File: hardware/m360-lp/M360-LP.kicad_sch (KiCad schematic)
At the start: 53 parts, among them J1 RJ45 SOLO, J2 RJ45 CLIMA/AUX, J3 J_VIN 3,0-6V, J4 M360-RF, Q1 AO3401A, Q2 AO3401A, SW1 Reed, U1 MCP1700T-3302E/TT, U2 74HC4051, U3 SRV05-4, U4 SRV05-4, U5 SRV05-4

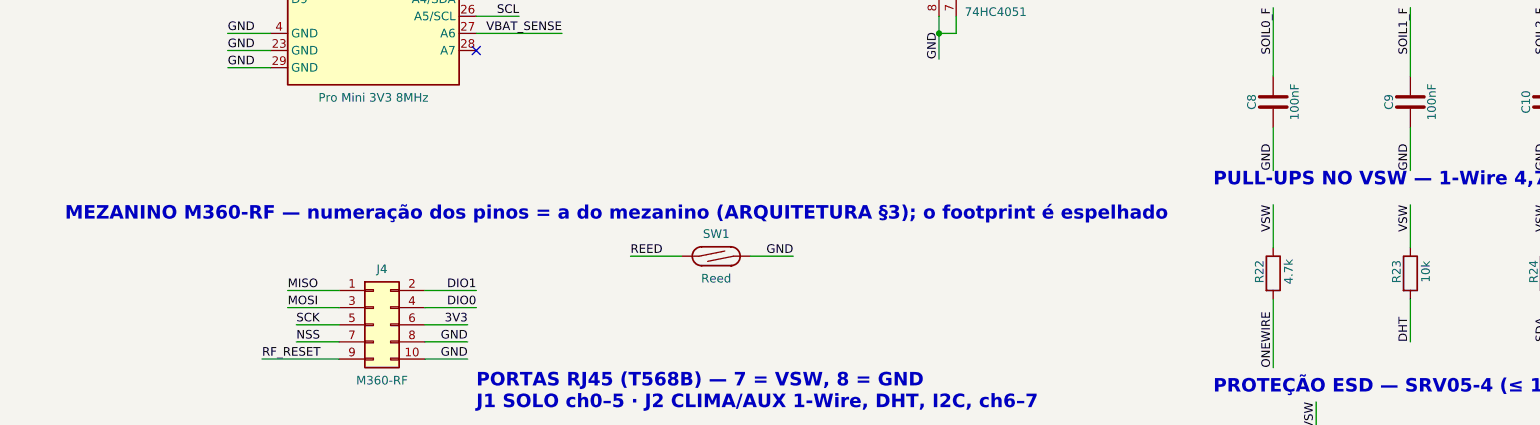
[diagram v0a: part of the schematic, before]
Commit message: feat(hardware): footprints da família e posicionamento da M360-LP na caixa
Biblioteca hardware/lib/M360.pretty com os quatro footprints que faltavam: Pro Mini,
soquete do mezanino, RJ45 (C385834) e reed (C315909). Os dois últimos vieram do LCSC pelo
easyeda2kicad, com os pinos-guia do RJ45 corrigidos para furo não metalizado e o modelo 3D
subido 6,3 mm — vinha atravessando a placa. O datasheet confirma conector comum: corpo de
12,6 mm apoiado na face e pinos de 3,0 mm.

O soquete do mezanino não precisa ser espelhado: o PinSocket stock já tem a coluna par em x
negativo, o mesmo lado em que ela fica no J1 do mezanino, que é montado na face de baixo.
Esquemático e documento corrigidos.

Furos livres do Pro Mini medidos por foto (docs/prominiFront.jpg), por homografia a partir
de quatro pinos de canto de posição conhecida (passo 2,54 mm, fileiras a 15,24 mm; escala
consistente em 2% nas quatro bordas): A5 em (12,70; 8,89), A4 em (12,70; 11,43) e GND/A6/A7
em x = 7,62/10,16/12,70 com y = 28,3 ± 0,3. Os espaçamentos medidos (2,57 e 2,59 mm)
confirmam a grade de 2,54. Esses cinco furos levam 1,2 mm — e não 1,0 — para absorver a
incerteza da medição; confirmar com paquímetro antes de fabricar.

Posicionamento em 86 × 62 mm, formato imposto pela caixa de 100 × 100 × 50 mm: o plugue
RJ45 é crimpado dentro da caixa e pede ~25-30 mm livres à frente dos conectores, com os
prensa-cabos na parede em frente. RJ45 e reed na borda de baixo, TVS logo atrás deles,
matriz RC dos 8 canais no meio, Pro Mini deitado com o header FTDI para fora da borda
esquerda, mezanino no alto à direita com o SMA pela borda e a alimentação embaixo dele
(~11 mm livres, só SMD baixo). DRC sem sobreposição de courtyard nem erro de isolamento;
faltam o roteamento e o acerto de serigrafia dos textos de U2, U4 e U5.

Co-Authored-By: Claude Opus 5 (1M context) <noreply@anthropic.com>
Claude-Session: https://claude.ai/code/session_01G3CpSsqAsoKgMUYE5MhRV7
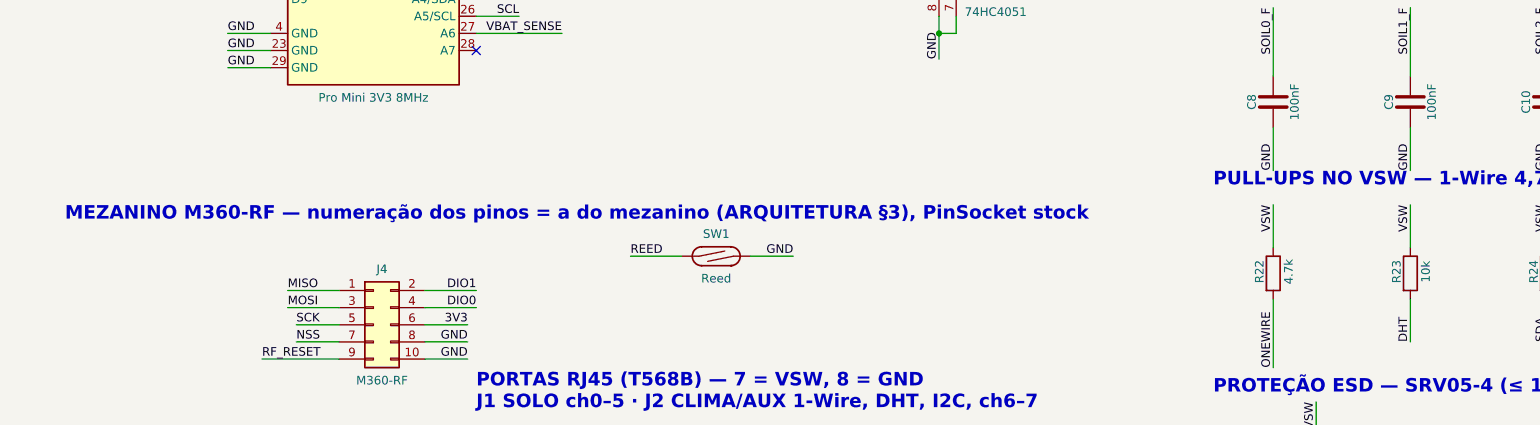
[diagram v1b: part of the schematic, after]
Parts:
- A1: footprint (none) -> M360:Arduino_ProMini_DeeKRobot
- J1, J2: footprint (none) -> M360:RJ45_R-RJ45R08P-A004
- J4: footprint (none) -> M360:M360-RF_Soquete_2x05
- SW1: footprint (none) -> M360:Reed_Littelfuse_59170
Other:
- note added: "MEZANINO M360-RF — numeração dos pinos = a do mezanino (ARQUITETURA §3), PinSocket stock"
- note removed: "MEZANINO M360-RF — numeração dos pinos = a do mezanino (ARQUITETURA §3); o footprint é espelhado"
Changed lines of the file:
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@@
 		(company "M360 Horta")
 		(comment 1 "Arquitetura: hardware/ARQUITETURA_FAMILIA.md §4 e §7")
-		(comment 2 "Footprints pendentes: A1 Pro Mini, J1/J2 RJ45, J4 soquete espelhado, SW1 reed")
+		(comment 2 "Footprints em hardware/lib/M360.pretty; furos A4–A7 do Pro Mini a medir")
 	)
-	(text "MEZANINO M360-RF — numeração dos pinos = a do mezanino (ARQUITETURA §3); o footprint é espelhado"
+	(text "MEZANINO M360-RF — numeração dos pinos = a do mezanino (ARQUITETURA §3), PinSocket stock"
 		(exclude_from_sim no)
 		(at 30.48 185.42 0)
@@
 			)
 		)
-		(property "Footprint" ""
+		(property "Footprint" "M360:M360-RF_Soquete_2x05"
 			(at 76.2 200.66 0)
 			(hide yes)
@@
 			)
 		)
-		(property "Footprint" ""
+		(property "Footprint" "M360:RJ45_R-RJ45R08P-A004"
 			(at 111.76 239.395 90)
 			(hide yes)
@@
 			)
 		)
-		(property "Footprint" ""
+		(property "Footprint" "M360:RJ45_R-RJ45R08P-A004"
 			(at 157.48 239.395 90)
 			(hide yes)
@@
 			)
 		)
-		(property "Footprint" ""
+		(property "Footprint" "M360:Arduino_ProMini_DeeKRobot"
 			(at 76.2 134.62 0)
 			(hide yes)
@@
 			)
 		)
-		(property "Footprint" ""
+		(property "Footprint" "M360:Reed_Littelfuse_59170"
 			(at 127 190.5 0)
 			(hide yes)

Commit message: feat(hardware): reed vira botão na LP e na ACT — esquemático apenas
⚠️ **ENTREGA PARCIAL: as placas NÃO acompanham.** Os dois `.kicad_pcb` continuam com o reed
`M360:Reed_Littelfuse_59170`. Sincronizar esquemático → placa vai trocar o footprint e
**invalidar o roteamento das duas** (§11.5). Não faça isso sem estar pronto para rerrotear.

O que entra aqui:

- SW1 passa de `Switch:SW_Reed` para `Switch:SW_Push`, footprint
  `Button_Switch_THT:SW_PUSH_6mm`, valor "Repareamento". Os dois símbolos têm pinagem e
  geometria idênticas (pinos 1 e 2 em ±5,08), então a troca não pode alterar a fiação — e o
  `netdiff.py` confirmou: LP 47 redes/182 nós e ACT 63/166, idênticas à base nas duas;
- `place_lp.py`: SW1 de (160, 158) para (160, 153) — o botão ocupa 9,6 × 7,6 mm contra
  11,5 × 2,4 do reed e, em 158, avançaria até y ≈ 164, além da borda em 162;
- `place_act.py`: SW1 sem rotação, e **J1 de rot 90 para rot 0**. O borne abre para −x (as guias
  de fio estão em x ≈ −5,68 no footprint), então em rot 90 a abertura apontava para dentro da
  placa;
- `.kicad_pro` das duas: `track_width` de 0,2 para 0,25 mm, o padrão da família (§11.2). O
  `set_design_rules` do MCP nunca persistiu esse valor — gravava o mínimo.

**Por que parou aqui.** A troca do footprint exige rerroteamento completo, que depende de
`export_dsn`/`import_ses` — e o servidor MCP travou no meio do trabalho: até `get_board_info`
passou a estourar 30 s, dez sondagens seguidas. O `kicad-cli` não exporta nem importa Specctra,
então não há contorno. As placas foram revertidas ao estado commitado e íntegro (LP 552
segmentos/48 vias, ACT 463/23, conferidos contra `bf701dc` e `e94779f`).

Ferramentas novas, todas nascidas deste trabalho:

- `clear_tracks.py` — apaga trilhas e vias para rerrotear do zero;
- `zone_thermals.py` — afina o alívio térmico das zonas;
- `gnd_stitch.py` — via de costura em ilha de plano solta, **com defeito conhecido e
  documentado**: o critério interno de "ilha já ligada" não prova ligação ao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
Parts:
- removed SW1: Reed, M360:Reed_Littelfuse_59170, symbol Switch:SW_Reed
- added SW1: Repareamento, Button_Switch_THT:SW_PUSH_6mm, symbol Switch:SW_Push
- C13: LCSC C14663 -> C315909
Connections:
- net GND: now also SW1.2
- net REED: now also SW1.1
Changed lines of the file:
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@@
 			)
 		)
-		(property "LCSC" "C14663"
+		(property "LCSC" "C315909"
 			(at 311.15 167.64 0)
 			(hide yes)
@@
 	)
 	(symbol
-		(lib_id "Switch:SW_Reed")
-		(at 127 190.5 0)
-		(unit 1)
-		(body_style 1)
-		(exclude_from_sim no)
-		(in_bom yes)
-		(on_board yes)
-		(in_pos_files yes)
-		(dnp no)
-		(property "Reference" "SW1"
-			(at 127 187.198 0)
-			(show_name no)
-			(do_not_autoplace no)
-			(effects
-				(font
-					(size 1.27 1.27)
-				)
-			)
-		)
-		(property "Value" "Reed"
-			(at 127 193.802 0)
-			(show_name no)
-			(do_not_autoplace no)
-			(effects
-				(font
-					(size 1.27 1.27)
-				)
-			)
-		)
-		(property "Footprint" "M360:Reed_Littelfuse_59170"
-			(at 127 190.5 0)
-			(hide yes)
-			(show_name no)
-			(do_not_autoplace no)
-			(effects
-				(font
-					(size 1.27 1.27)
-				)
-			)
-		)
-		(property "Datasheet" ""
-			(at 127 190.5 0)
-			(hide yes)
-			(show_name no)
-			(do_not_autoplace no)
-			(effects
-				(font
-					(size 1.27 1.27)
-				)
-			)
-		)
-		(property "Description" "reed switch"
-			(at 127 190.5 0)
-			(hide yes)
-			(show_name no)
-			(do_not_autoplace no)
-			(effects
-				(font
-					(size 1.27 1.27)
-				)
-			)
-		)
-		(property "LCSC" "C315909"
-			(at 127 190.5 0)
-			(hide yes)
-			(show_name no)
-			(do_not_autoplace no)
-			(effects
-				(font
-					(size 1.27 1.27)
-				)
-			)
-		)
-		(pin "1"
-		)
-		(pin "2"
-		)
-		(instances
-			(project "M360-LP"
-				(path "/e985d55b-0fcb-4497-9a07-fdd20db72e7e"
-					(reference "SW1")
-					(unit 1)
-				)
-			)
-		)
-	)
-	(symbol
 		(lib_id "Device:R")
 		(at 116.84 111.76 0)
@@
 		)
 	)
+	(symbol
+		(lib_id "Switch:SW_Push")
+		(at 127 190.5 0)
+		(unit 1)
+		(body_style 1)
+		(exclude_from_sim no)
+		(in_bom yes)
+		(on_board yes)
+		(in_pos_files yes)
+		(dnp no)
+		(property "Reference" "SW1"
+			(at 128.27 193.04 0)
+			(show_name no)
+			(do_not_autoplace no)
+			(effects
+				(font
+					(size 1.27 1.27)
+				)
+				(justify left)
+			)
+		)
+		(property "Value" "Repareamento"
+			(at 127 188.976 0)
+			(show_name no)
+			(do_not_autoplace no)
+			(effects
+				(font
+					(size 1.27 1.27)
+				)
+			)
+		)
+		(property "Footprint" "Button_Switch_THT:SW_PUSH_6mm"
+			(at 127 195.58 0)
+			(hide yes)
+			(show_name no)
+			(do_not_autoplace no)
+			(effects
+				(font
+					(size 1.27 1.27)
+				)
+			)
+		)
+		(property "Datasheet" ""
+			(at 127 195.58 0)
+			(hide yes)
+			(show_name no)
+			(do_not_autoplace no)
+			(effects
+				(font
+					(size 1.27 1.27)
+				)
+			)
+		)
+		(property "Description" "Push button switch, generic, two pins"
+			(at 127 190.5 0)
+			(hide yes)
+			(show_name no)
+			(do_not_autoplace no)
+			(effects
+				(font
+					(size 1.27 1.27)
+				)
+			)
+		)
+		(pin "1"
+		)
+		(pin "2"
+		)
+		(instances
+			(project "M360-LP"
+				(path "/e985d55b-0fcb-4497-9a07-fdd20db72e7e"
+					(reference "SW1")
+					(unit 1)
+				)
+			)
+		)
+	)

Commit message: feat(hardware): LP e ACT rerroteadas com o botão; GND volta a ser roteado
Conclui a troca do reed pelo botão iniciada em 0948368, que parou no esquemático.

Placas, para cada uma: del_fp.py SW1 → sincronização com o esquemático → place_*.py →
clear_tracks.py → export_dsn → dsn_sem_plano.py → Freerouting → import_ses →
zone_thermals.py → DRC com refill.

- M360-LP: 572 trilhas, 44 vias. DRC com 0 erros e 0 desconectados; restam os 8
  silk_edge_clearance dos RJ45, que já existiam.
- M360-ACT: 489 trilhas, 24 vias. DRC com 0 erros e 0 desconectados; restam os 13
  silk_edge_clearance, que já existiam. J1 em rot 0, como o place_act.py já pedia.
- Redes de todos os pads conferidas contra o HEAD: só o SW1 mudou. Trilhas todas de 0,25 mm.
- Paridade esquemático × placa com as mesmas contagens da base (237 e 195); some o
  footprint_symbol_mismatch do SW1.

**O GND não era roteado — e era isso que partia o plano.** Com zona de GND na placa, o DSN
declara `plane GND` e o Freerouting não desenha um fio de terra sequer. O primeiro roteamento
(bf701dc, 88 segmentos de GND) foi feito antes de as zonas existirem; todo rerroteamento
posterior perdia esse terra. Rerroteada com o DSN como sai do KiCad, a LP deu 16
unconnected_items, todos "Zona [GND]"; tirando as declarações plane, 0 — 100 segmentos de GND
na LP e 95 na ACT. Explica também os 15 desconectados imóveis da sessão anterior (§11.6).
Novo `tools/dsn_sem_plano.py`, e a §11 corrigida: 11.2, 11.4, 11.5 e 11.6.

Ajustes que o DRC pediu depois do rerroteamento:
- J4 da ACT, pino 8: starved_thermal → ligação sólida (pad_zone_connect.py), como o J3;
- silk_lp.py: referência do SW1 saía sobre "M360-LP"; vai para (172, 155);
- silk_act.py: referência do U1 encostava no J1, agora em rot 0; sobe para y = 143.

Botão: SHOU HAN TS665CJ, C393938, tátil 6 × 6 mm THT, SW1 nas três placas (LP, ACT e GW),
**solda manual e fora do PCBA**. Propriedade LCSC gravada nos três esquemáticos, com netlists
idênticas antes e depois. `add_lcsc.py` g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
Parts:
- SW1: LCSC (none) -> C393938
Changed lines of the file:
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@@
+			)
+		)
+		(property "LCSC" "C393938"
+			(at 127 190.5 0)
+			(hide yes)
+			(effects
+				(font
+					(size 1.27 1.27)
+				)
 			)
 		)

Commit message: feat(hardware): peças de solda manual fora do BOM e da posição; C13 da LP corrigido
Novo `tools/solda_manual.py`: marca as duas pontas pela referência — `in_bom no` e
`in_pos_files no` no símbolo, `exclude_from_bom` e `exclude_from_pos_files` no footprint. O BOM
sai do esquemático e a posição sai da placa; marcar um lado só faria a paridade divergir.

Aplicado:
- LP: SW1, J1, J2, A1, J4
- ACT: SW1, J3, J4, J5, A1, J2
- GW: SW1, J1

Conferido exportando BOM e posição antes e depois: saíram exatamente essas peças. Netlists
idênticas nas três; DRC e paridade com as mesmas contagens da base (LP 237, ACT 195, GW 69).
A propriedade LCSC fica nos símbolos, para a compra (§9.1).

**Defeito corrigido:** o C13 da LP (100 nF 0603) carregava o código do reed, C315909, desde
bc651ca — a JLCPCB montaria um reed no lugar do capacitor. Agora C14663, como os demais 100 nF,
pelo `add_lcsc.py --set`.

Também na §9.1: espaçamento de 6,5 × 4,5 mm do TS665CJ confirmado contra o datasheet.

Registrado na §9, sem correção: a ACT e a GW não têm código LCSC em peça nenhuma, e os
PWR_FLAG da GW saem no BOM. Bornes (J1 da ACT, J2 da GW) e JST (J3 da LP e da GW) continuam no
BOM, por não estarem na lista desta decisão.

Co-Authored-By: Claude Opus 5 (1M context) <noreply@anthropic.com>
Claude-Session: https://claude.ai/code/session_012t7RkcrXvvpDVjKVimNu18
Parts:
- A1, J1, J2, J4, SW1: now left out of the parts list
- C13: LCSC C315909 -> C14663
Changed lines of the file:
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@@
 			)
 		)
-		(property "Datasheet" ""
+		(property "LCSC" "C14663"
 			(at 311.15 167.64 0)
 			(hide yes)
-			(show_name no)
-			(do_not_autoplace no)
 			(effects
 				(font
@@
 			)
 		)
-		(property "Description" "Unpolarized capacitor"
+		(property "Datasheet" ""
 			(at 311.15 167.64 0)
 			(hide yes)
@@
 			)
 		)
-		(property "LCSC" "C315909"
+		(property "Description" "Unpolarized capacitor"
 			(at 311.15 167.64 0)
 			(hide yes)
@@
 		(body_style 1)
 		(exclude_from_sim no)
-		(in_bom yes)
+		(in_bom no)
 		(on_board yes)
-		(in_pos_files yes)
+		(in_pos_files no)
 		(dnp no)
 		(property "Reference" "J4"
@@
 		(body_style 1)
 		(exclude_from_sim no)
-		(in_bom yes)
+		(in_bom no)
 		(on_board yes)
-		(in_pos_files yes)
+		(in_pos_files no)
 		(dnp no)
 		(property "Reference" "J1"
@@
 		(body_style 1)
 		(exclude_from_sim no)
-		(in_bom yes)
+		(in_bom no)
 		(on_board yes)
-		(in_pos_files yes)
+		(in_pos_files no)
 		(dnp no)
 		(property "Reference" "J2"
@@
 		(body_style 1)
 		(exclude_from_sim no)
-		(in_bom yes)
+		(in_bom no)
 		(on_board yes)
-		(in_pos_files yes)
+		(in_pos_files no)
 		(dnp no)
 		(property "Reference" "A1"
@@
 		(body_style 1)
 		(exclude_from_sim no)
-		(in_bom yes)
+		(in_bom no)
 		(on_board yes)
-		(in_pos_files yes)
+		(in_pos_files no)
 		(dnp no)
 		(property "Reference" "SW1"

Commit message: feat(hardware): esquemáticos corrigidos após análise adversarial; reed nas três placas; GW em SMD
⚠️ **Só esquemáticos.** Os três .kicad_pcb estão defasados e serão refeitos depois de uma nova
análise adversarial, até zerar os achados (pedido do usuário). ARQUITETURA §9 registra.

Correções da revisão (Fable 5.1, 2026-09-13):
- ACT #1: A6 da J5 com divisor 10 k (R5) / 20 k (R6) + 100 nF (C8); J5.3 e U8.3 vão para AUX_A6_IN.
  Antes, 5 V do par marrom chegavam direto ao ADC6 de um ATmega a 3,3 V.
- ACT #2: pull-up do /OE (R2) de +5V para 3V3 — A5 em alta impedância ficava a ~3,8 V.
- ACT #4: 7× 100 kΩ — pull-down em MUX_S0..S3, pull-up para 5 V em MUX_SIG/REL_NFT/REL_OXI.
- ACT #6: AMS1117 → ME6211C33M5 (C82942), estável com cerâmico.
- ACT #12: AO3401A (Q1) contra inversão no borne; J1.1 vai para VIN_RAW.
- GW #5/#12: Schottky SS14 (D1, C2480) em série de J2.1 (VIN_RAW) para +5V.
- Achados 3, 7, 8, 9, 10 e 11: documentação e regras de firmware (módulo TP4056 com DW01+8205;
  vazão com INPUT; calibração e analogReference do A6 da LP; chave do mezanino cortando o pino 10;
  FTDI sem VCC; orçamento do 3,3 V da GW).

Decisões do usuário:
- Reed switch Littelfuse 59170 (C315909) de volta na LP e na ACT e **no lugar do botão AP/reset da
  GW**, pela PCBA. Símbolo trocado por texto (pinagem idêntica): netlists idênticas.
- GW em SMD pela JLCPCB: R 0603, C1 10 µF 0805 (`Device:C`), C2–C4 100 nF 0603, códigos basic.
  Solda manual só U1 (D1 mini), J1, J2, J3. Os PWR_FLAG saem do BOM.
- Solda manual marcada só nos esquemáticos (`solda_manual.py --so-esquematico`, e `--desfazer` no
  SW1): LP J3; ACT J1; GW U1, J1, J2, J3.

Verificado nas três: netdiff contra a base lista só as mudanças acima (LP idêntica); campos de
todos os componentes comparados; símbolos de biblioteca embutidos comparados com o HEAD; ERC 0;
BOM com código LCSC em todas as linhas (exceto módulos); desenho conferido em PDF.

Três armadilhas medidas no caminho (ARQUITETURA §12):
- `replace_schematic_component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
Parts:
- J3: now left out of the parts list
- SW1: value Repareamento -> Reed; footprint Button_Switch_THT:SW_PUSH_6mm -> M360:Reed_Littelfuse_59170; symbol Switch:SW_Push -> Switch:SW_Reed; LCSC C393938 -> C315909; now in the parts list
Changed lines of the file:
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@@
 		(body_style 1)
 		(exclude_from_sim no)
-		(in_bom yes)
+		(in_bom no)
 		(on_board yes)
-		(in_pos_files yes)
+		(in_pos_files no)
 		(dnp no)
 		(property "Reference" "J3"
@@
 	)
 	(symbol
-		(lib_id "Switch:SW_Push")
+		(lib_id "Switch:SW_Reed")
 		(at 127 190.5 0)
 		(unit 1)
 		(body_style 1)
 		(exclude_from_sim no)
-		(in_bom no)
+		(in_bom yes)
 		(on_board yes)
-		(in_pos_files no)
+		(in_pos_files yes)
 		(dnp no)
 		(property "Reference" "SW1"
@@
 			)
 		)
-		(property "Value" "Repareamento"
+		(property "Value" "Reed"
 			(at 127 188.976 0)
 			(show_name no)
@@
 			)
 		)
-		(property "Footprint" "Button_Switch_THT:SW_PUSH_6mm"
+		(property "Footprint" "M360:Reed_Littelfuse_59170"
 			(at 127 195.58 0)
 			(hide yes)
@@
 			)
 		)
-		(property "LCSC" "C393938"
+		(property "LCSC" "C315909"
 			(at 127 190.5 0)
 			(hide yes)
@@
 			)
 		)
-		(property "Description" "Push button switch, generic, two pins"
+		(property "Description" "reed switch"
 			(at 127 190.5 0)
 			(hide yes)

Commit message: fix(hardware): esquemáticos — correções da 3ª análise adversarial
⚠️ Só esquemáticos; as placas continuam defasadas de propósito até zerar os achados.

- LP #1: 100 Ω em série (R26–R29, C22775) entre o TVS e o Pro Mini nas linhas de campo digitais.
  A1.18/19/25/26 passam às redes ONEWIRE_MCU, DHT_MCU, SDA_MCU e SCL_MCU; pull-ups e TVS ficam do
  lado do conector. O pino do ATmega deixa de dividir o surto com o TVS.
- ACT #2: 100 Ω em série (R21–R32) entre o CI e o TVS nas 12 linhas de relé — U3 I0–I9 em
  REL_CHx_MUX, U2 2Y1/2Y2 em REL_NFT_BUF/REL_OXI_BUF. Custa 0,2 V nos 2 mA do opto.
- ACT e GW #3: TVS SMAJ5.0A (D2, C2925443) do +5V ao GND, depois do Q1 (ACT) e do D1 (GW), contra
  DC-DC ajustável girado por engano. Símbolo `Device:D_Zener` — o `D_TVS` do KiCad é bidirecional.
- GW #4: nota — o LED azul do D1 mini no GPIO2 fica invertido em relação ao verde do painel.
- Regras: limiar de corte de TX ≥ 3,0 V por causa do BOD de 2,7 V (efuse 0xFD); confirmar os fuses
  dos clones DeeKRobot por ISP; `initLEDs` com argumentos trocados continua registrado. §9.

Verificado: netdiff contra o commit anterior só com as redes previstas (LP 8, ACT 26, GW 2);
campos dos componentes existentes inalterados; símbolos de biblioteca existentes inalterados
(entra só o D_Zener, sai o D_TVS); ERC 0; BOM com código LCSC em todas as linhas; desenho
conferido em PDF. O diff da LP é grande porque o arquivo passou pela primeira vez por
`kicad-cli sch upgrade --force` (§12).

No caminho: o MCP ignorou o ângulo pedido em `add_schematic_component` (todas as peças entraram em
rot 0) e, com as fileiras apertadas, os fios desenhados fundiram redes — o netdiff e o ERC pegaram,
e a geometria foi refeita antes do commit.

Co-Authored-By: Claude Opus 5 (1M context) <noreply@anthropic.com>
Claude-Session: https://claude.ai/code/session_012t7RkcrXvvpDVjKVimNu18
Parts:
- added R26, R27, R28, R29: 100, Resistor_SMD:R_0603_1608Metric, symbol Device:R
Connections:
- net DHT: now also R27.2; no longer A1.19 (A2)
- net ONEWIRE: now also R26.2; no longer A1.18 (A1)
- net SCL: now also R29.2; no longer A1.26 (A5/SCL)
- net SDA: now also R28.2; no longer A1.25 (A4/SDA)
- new net DHT_MCU: A1.19 (A2), R27.1
- new net ONEWIRE_MCU: A1.18 (A1), R26.1
- new net SCL_MCU: A1.26 (A5/SCL), R29.1
- new net SDA_MCU: A1.25 (A4/SDA), R28.1
